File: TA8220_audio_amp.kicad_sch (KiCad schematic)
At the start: 24 parts, among them J1 Input, J2 Output, J3 Power

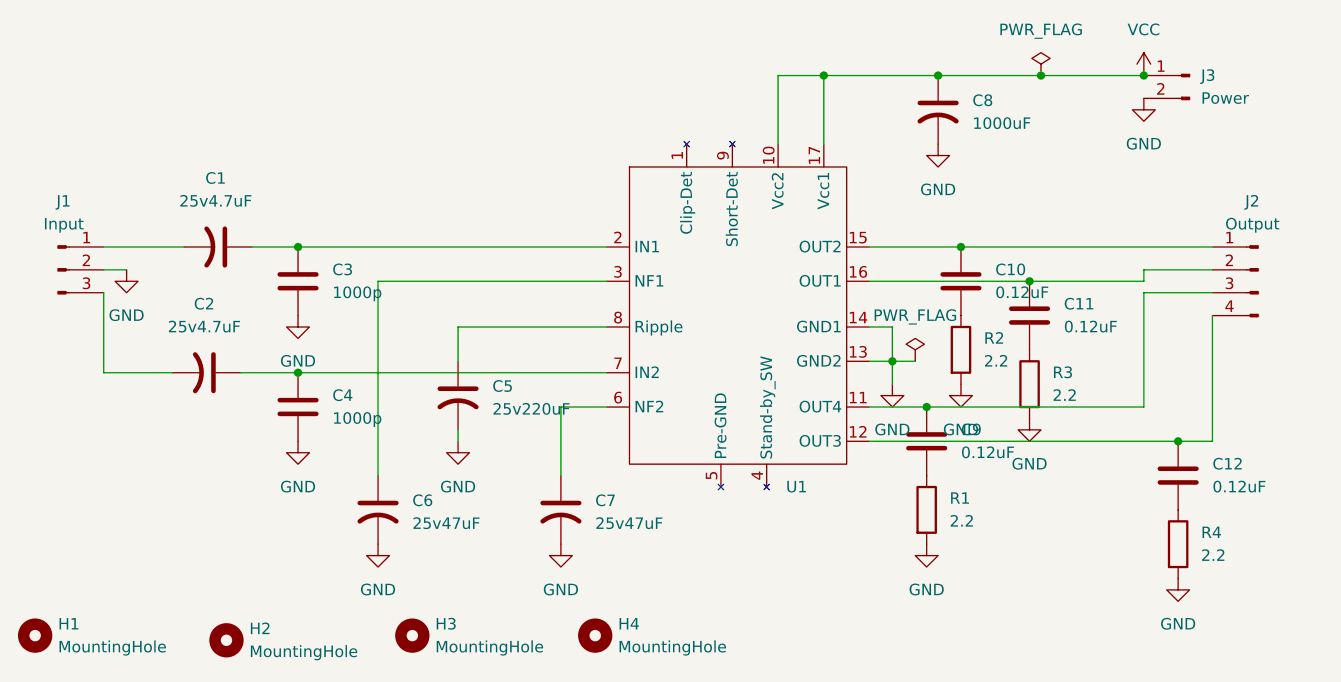
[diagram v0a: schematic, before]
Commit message: http://vicdiy.com/products/TV_linked_amp2/linked_amp2.html を参考に利得を下げるよう部品を変更
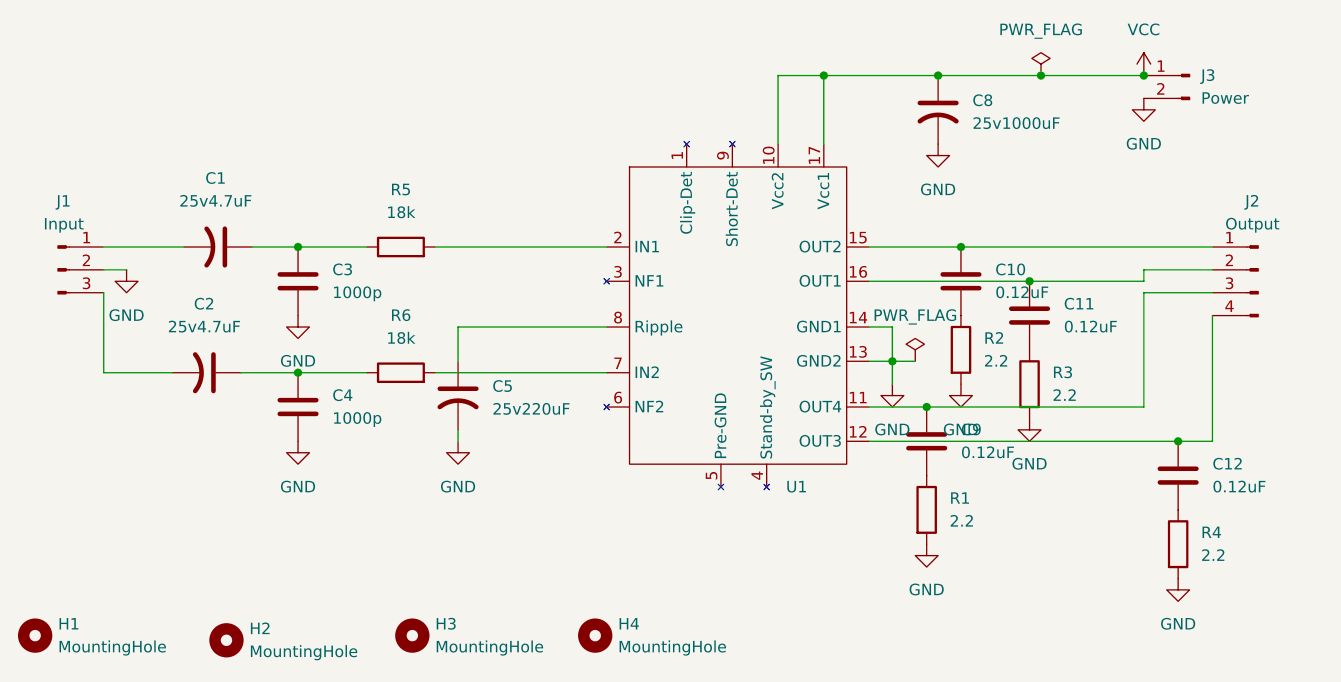
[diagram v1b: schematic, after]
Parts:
- removed C6, C7: 25v47uF, Capacitor_THT:CP_Radial_D5.0mm_P2.50mm, symbol Device:C_US
- added R5: 18k, Resistor_THT:R_Axial_DIN0411_L9.9mm_D3.6mm_P15.24mm_Horizontal, symbol Device:R
- added R6: 18k, Resistor_THT:R_Axial_DIN0411_L9.9mm_D3.6mm_P12.70mm_Horizontal, symbol Device:R
- C8: value 1000uF -> 25v1000uF
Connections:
- net at C2.1, C4.1: now also R6.1; no longer U1.7 (IN2)
- net at C1.1, C3.1: now also R5.1; no longer U1.2 (IN1)
- new net: R6.2, U1.7 (IN2)
- new net: R5.2, U1.2 (IN1)

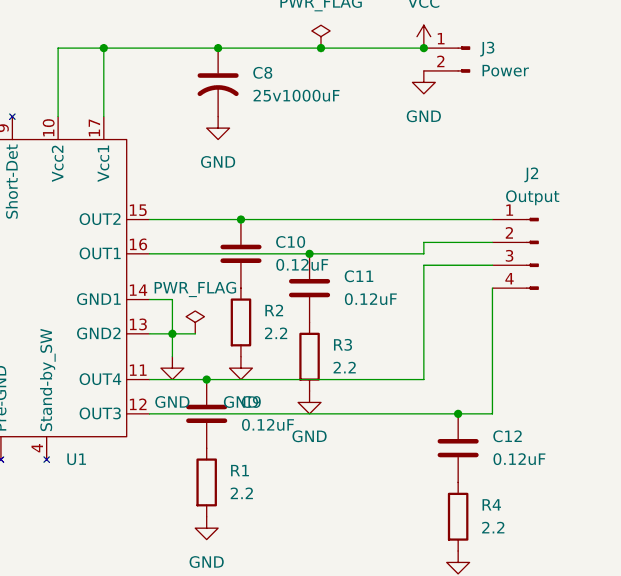
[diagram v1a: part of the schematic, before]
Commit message: パッド径を2に修正
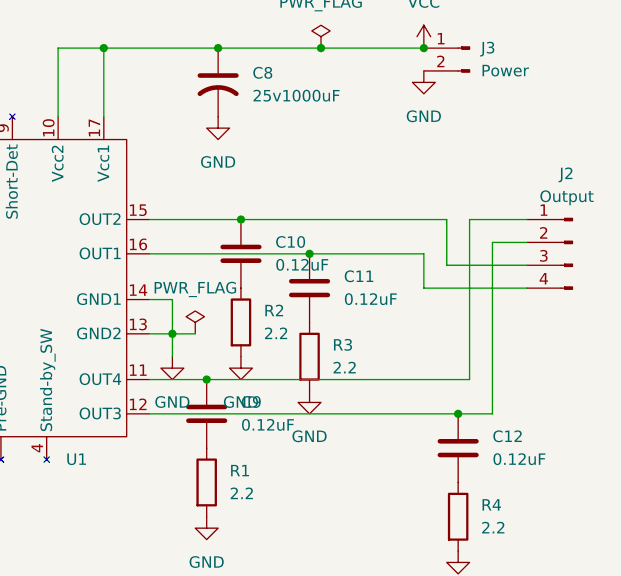
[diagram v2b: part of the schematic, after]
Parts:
- R5: footprint Resistor_THT:R_Axial_DIN0411_L9.9mm_D3.6mm_P15.24mm_Horizontal -> Resistor_THT:R_Axial_DIN0617_L17.0mm_D6.0mm_P20.32mm_Horizontal
- R6: footprint Resistor_THT:R_Axial_DIN0411_L9.9mm_D3.6mm_P12.70mm_Horizontal -> Resistor_THT:R_Axial_DIN0617_L17.0mm_D6.0mm_P20.32mm_Horizontal
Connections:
- net at C9.1, U1.11 (OUT4): now also J2.1 (Pin_1); no longer J2.3 (Pin_3)
- net at C12.1, U1.12 (OUT3): now also J2.2 (Pin_2); no longer J2.4 (Pin_4)
- net at C10.1, U1.15 (OUT2): now also J2.3 (Pin_3); no longer J2.1 (Pin_1)
- net at C11.1, U1.16 (OUT1): now also J2.4 (Pin_4); no longer J2.2 (Pin_2)
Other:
- moved on the sheet: J2
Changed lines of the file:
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@@
+	)
+	(junction
+		(at 124.46 76.2)
+		(diameter 0)
+		(color 0 0 0 0)
 	)
 	(junction
@@
 	)
 	(junction
-		(at 124.46 76.2)
-		(diameter 0)
-		(color 0 0 0 0)
-	)
-	(junction
 		(at 132.08 80.01)
 		(diameter 0)
@@
 	(wire
 		(pts
+			(xy 144.78 83.82) (xy 156.21 83.82)
+		)
+		(stroke
+			(width 0)
+			(type default)
+		)
+	)
+	(wire
+		(pts
 			(xy 121.92 57.15) (xy 133.35 57.15)
 		)
@@
 	(wire
 		(pts
-			(xy 152.4 81.28) (xy 144.78 81.28)
-		)
-		(stroke
-			(width 0)
-			(type default)
-		)
-	)
-	(wire
-		(pts
 			(xy 50.8 90.17) (xy 58.42 90.17)
 		)
@@
 	(wire
 		(pts
+			(xy 124.46 76.2) (xy 147.32 76.2)
+		)
+		(stroke
+			(width 0)
+			(type default)
+		)
+	)
+	(wire
+		(pts
 			(xy 44.45 90.17) (xy 50.8 90.17)
 		)
@@
 	(wire
 		(pts
+			(xy 149.86 76.2) (xy 156.21 76.2)
+		)
+		(stroke
+			(width 0)
+			(type default)
+		)
+	)
+	(wire
+		(pts
 			(xy 104.14 64.77) (xy 104.14 57.15)
 		)
@@
 	(wire
 		(pts
+			(xy 152.4 78.74) (xy 152.4 97.79)
+		)
+		(stroke
+			(width 0)
+			(type default)
+		)
+	)
+	(wire
+		(pts
 			(xy 133.35 57.15) (xy 144.78 57.15)
 		)
@@
 	(wire
 		(pts
+			(xy 147.32 81.28) (xy 156.21 81.28)
+		)
+		(stroke
+			(width 0)
+			(type default)
+		)
+	)
+	(wire
+		(pts
 			(xy 114.3 93.98) (xy 120.65 93.98)
 		)
@@
 	(wire
 		(pts
-			(xy 152.4 83.82) (xy 152.4 97.79)
-		)
-		(stroke
-			(width 0)
-			(type default)
-		)
-	)
-	(wire
-		(pts
-			(xy 144.78 81.28) (xy 144.78 93.98)
-		)
-		(stroke
-			(width 0)
-			(type default)
-		)
-	)
-	(wire
-		(pts
 			(xy 29.21 81.28) (xy 29.21 90.17)
 		)
@@
 	(wire
 		(pts
+			(xy 149.86 76.2) (xy 149.86 93.98)
+		)
+		(stroke
+			(width 0)
+			(type default)
+		)
+	)
+	(wire
+		(pts
 			(xy 114.3 80.01) (xy 132.08 80.01)
 		)
@@
 	(wire
 		(pts
+			(xy 147.32 76.2) (xy 147.32 81.28)
+		)
+		(stroke
+			(width 0)
+			(type default)
+		)
+	)
+	(wire
+		(pts
 			(xy 66.04 76.2) (xy 85.09 76.2)
 		)
@@
 	(wire
 		(pts
-			(xy 144.78 78.74) (xy 144.78 80.01)
+			(xy 144.78 80.01) (xy 144.78 83.82)
 		)
 		(stroke
@@
 	(wire
 		(pts
-			(xy 124.46 76.2) (xy 152.4 76.2)
-		)
-		(stroke
-			(width 0)
-			(type default)
-		)
-	)
-	(wire
-		(pts
 			(xy 114.3 76.2) (xy 124.46 76.2)
 		)
@@
 	(wire
 		(pts
-			(xy 120.65 93.98) (xy 144.78 93.98)
+			(xy 120.65 93.98) (xy 149.86 93.98)
 		)
 		(stroke
@@
 	(wire
 		(pts
-			(xy 152.4 78.74) (xy 144.78 78.74)
-		)
-		(stroke
-			(width 0)
-			(type default)
-		)
-	)
-	(wire
-		(pts
 			(xy 116.84 85.09) (xy 116.84 88.9)
+		)
+		(stroke
+			(width 0)
+			(type default)
+		)
+	)
+	(wire
+		(pts
+			(xy 156.21 78.74) (xy 152.4 78.74)
 		)
 		(stroke
@@
 			)
 		)
-		(property "Footprint" "Resistor_THT:R_Axial_DIN0411_L9.9mm_D3.6mm_P12.70mm_Horizontal"
+		(property "Footprint" "Resistor_THT:R_Axial_DIN0617_L17.0mm_D6.0mm_P20.32mm_Horizontal"
 			(at 62.23 91.948 90)
 			(effects
@@
 			)
 		)
-		(property "Footprint" "Resistor_THT:R_Axial_DIN0411_L9.9mm_D3.6mm_P15.24mm_Horizontal"
+		(property "Footprint" "Resistor_THT:R_Axial_DIN0617_L17.0mm_D6.0mm_P20.32mm_Horizontal"
 			(at 62.23 77.978 90)
 			(effects
@@
 	(symbol
 		(lib_id "Connector:Conn_01x04_Pin")
-		(at 157.48 78.74 0)
+		(at 161.29 78.74 0)
 		(mirror y)
 		(unit 1)
@@
 		(dnp no)
 		(property "Reference" "J2"
-			(at 156.845 71.12 0)
+			(at 160.655 71.12 0)
 			(effects
 				(font
@@
 		)
 		(property "Value" "Output"
-			(at 156.845 73.66 0)
+			(at 160.655 73.66 0)
 			(effects
 				(font
@@
 		)
 		(property "Footprint" "Connector_JST:JST_XH_B4B-XH-A_1x04_P2.50mm_Vertical"
-			(at 157.48 78.74 0)
+			(at 161.29 78.74 0)
 			(effects
 				(font
@@
 		)
 		(property "Datasheet" "~"
-			(at 157.48 78.74 0)
+			(at 161.29 78.74 0)
 			(effects
 				(font
@@
 		)
 		(property "Description" "Generic connector, single row, 01x04, script generated"
-			(at 157.48 78.74 0)
-			(effects
-				(font
+			(at 161.29 78.74 0)
+			(effects
+				(font

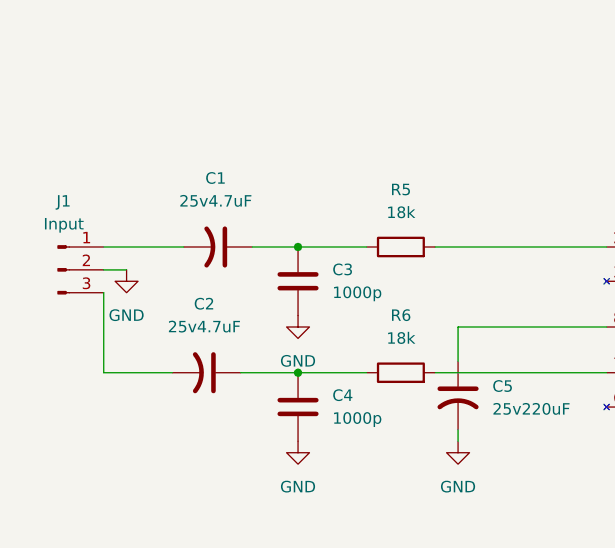
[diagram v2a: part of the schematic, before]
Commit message: C1,C2を4.7 -> 0.47に修正
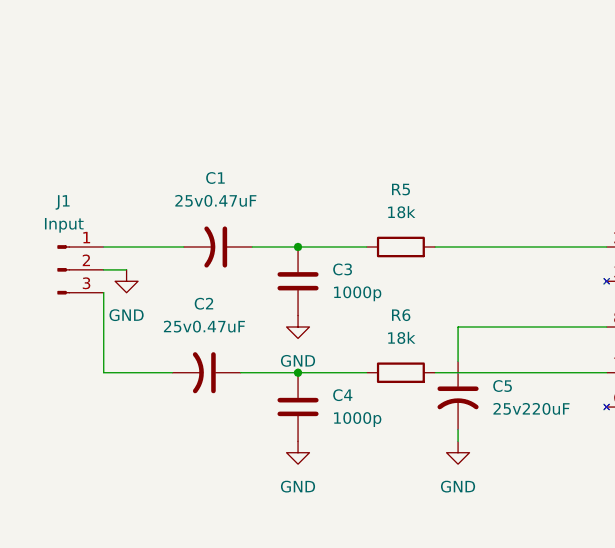
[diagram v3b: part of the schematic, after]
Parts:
- C1, C2: value 25v4.7uF -> 25v0.47uF
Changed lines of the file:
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@@
 			)
 		)
-		(property "Value" "25v4.7uF"
+		(property "Value" "25v0.47uF"
 			(at 41.656 71.12 90)
 			(effects
@@
 			)
 		)
-		(property "Value" "25v4.7uF"
+		(property "Value" "25v0.47uF"
 			(at 40.386 85.09 90)
 			(effects

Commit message: データシートどおりに作り直し
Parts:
- removed R5, R6: 18k, Resistor_THT:R_Axial_DIN0617_L17.0mm_D6.0mm_P20.32mm_Horizontal, symbol Device:R
- added C6, C7: 25v47uF, Capacitor_THT:CP_Radial_D5.0mm_P2.50mm, symbol Device:C_US
- C1, C2: value 25v0.47uF -> 25v4.7uF
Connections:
- net GND: now also C6.2, C7.2
- net VCC: now also U1.4 (Stand-by_SW)
- net at C2.1, C4.1: now also U1.7 (IN2)
- net at C1.1, C3.1: now also U1.2 (IN1)
- net at U1.3 (NF1): now also C6.1
- net at U1.6 (NF2): now also C7.1
